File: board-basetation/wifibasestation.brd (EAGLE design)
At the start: 50 x 23 mm, 25 parts, among them J1 SWD_SHROUD_SMD, Q1 MOSFET-PCHANNELSMD

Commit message: some routing
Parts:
- removed C7: (no value), rcl:C0603K
- removed Q1: MOSFET-PCHANNELSMD, SparkFun-DiscreteSemi:SOT23-3
- added C10, C11, C8, C9: (no value), rcl:C0603K
- added IC1: 1117EMP, dtb:SOT223
- added IC2: HTU21D, Mine:DFN6-L
- added R5: (no value), rcl:R0603
- added S1: SWITCH-MOMENTARY-2SMD, Mine:TACTILE_SWITCH_SMD
- added U$4: BUS-SMA, Ava:BUS-SMA
- LED1, LED2, LED3: device dtb:1206 -> led:CHIP-LED0805
- U$3: value CRYSTAL-GROUNDED -> LMT85; device SparkFun-FreqCtrl:CRYSTAL-SMD-5X3 -> Mine:SC70-5L
- moved R1 126.0 mm to (40.4, 8.89), turned to 90 degrees
- moved C6 123.2 mm to (46.2, 2.29)
- moved R2 115.8 mm to (28.4, 3.76), turned to 180 degrees
- moved C4 109.9 mm to (29.8, 16.3), turned to 270 degrees
- moved C5 107.6 mm to (29.3, 8.95), turned to 270 degrees
- moved C3 99.5 mm to (18.0, 18.7)
- moved C1 98.4 mm to (27.4, 8.95), turned to 270 degrees
- moved C2 91.5 mm to (16.5, 10.5), turned to 90 degrees
- moved U$2 24.5 mm to (14.0, 19.4), turned to 180 degrees
- moved U$3 14.8 mm to (35.6, 24.1)
- moved JP3 5.04 mm to (17.7, 21.0)
- moved RN1 4.84 mm to (32.3, 8.38)
- moved LED1 4.67 mm to (36.3, 4.32)
- moved R3 4.19 mm to (15.5, 14.3), turned to 180 degrees
- moved R4 4.12 mm to (8.62, 10.2)
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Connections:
- removed net N$1: SV1.1
- removed net N$6: SV1.7
- new net CH_PD: SV1.6, U$1.5
- new net DIO0: U$1.45, U$2.DIO0
- new net I2C2_SCL: IC2.6, R1.1, U$1.21
- new net I2C2_SDA: IC2.1, R5.1, U$1.22
- new net MISO: U$1.40, U$2.MISO
- new net MOSI: U$1.41, U$2.MOSI
- new net N$19: U$2.ANT, U$4.1
- new net N$20: LED3.A, RN1.5
- new net N$21: RN1.3, U$1.3
- new net N$22: RN1.2, U$1.4
- new net N$23: U$1.29
- new net N$24: U$1.30
- new net N$26: U$1.26
- new net N$27: U$1.27
- new net NSS: U$1.46, U$2.NSS
- new net RST: U$2.RESET
- new net SCK: U$1.39, U$2.SCK
- new net USART1_RX: SV1.8, U$1.43
- new net USART1_TX: SV1.1, U$1.42
- new net USART2_RX: JP3.TXO, U$1.13
- new net USART2_TX: JP3.RXI, U$1.12
- new net W_RST: SV1.4, U$1.6
- net +3V3: now also C10.1, C11.1, C6.1, C9.1, IC1.2, IC1.4, IC2.5, JP3.VCC, R1.2, R5.2, S1.3, SV1.2, U$2.VCC
- net GND: now also C10.2, C11.2, C8.2, C9.2, IC1.1, IC2.2, JP3.GND, LED1.C, LED2.C, LED3.C, SV1.7, U$2.GNDA, U$2.GNDB, U$4.2, U$4.3, U$4.4, U$4.5; no longer C7.2, U$3.2, U$3.4
- net N$10: now also LED2.A, RN1.6; no longer Q1.2
- net N$12: now also U$1.15; no longer C7.1, R1.2, U$3.3
- net N$14: now also U$1.16; no longer R1.1, U$1.6
- net N$15: now also S1.1
- net N$16: now also U$1.17; no longer C6.1, U$1.5, U$3.1
- net N$2: now also RN1.4, U$1.2; no longer Q1.3, SV1.2
- net N$3: now also U$1.10; no longer SV1.4
- net N$7: now also U$1.11; no longer SV1.6
- net N$8: now also U$1.14; no longer SV1.8
- net N$9: now also LED1.A, RN1.7, RN1.8; no longer Q1.1
- net VBUS: now also C8.1, IC1.3
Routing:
- net +3V3: track 0.00 -> 137.7 mm, vias 0 -> 18
- net GND: track 0.00 -> 65.9 mm, vias 0 -> 13
- net NRST: track 0.00 -> 43.6 mm, vias 0 -> 2
- net USART1_RX: track 0.00 -> 43.3 mm, vias 0 -> 2
- net USART1_TX: track 0.00 -> 37.1 mm, vias 0 -> 1
- net I2C2_SCL: track 0.00 -> 37.1 mm, vias 0 -> 4
- net I2C2_SDA: track 0.00 -> 33.1 mm, vias 0 -> 4
- net N$15: track 0.00 -> 32.4 mm, vias 0 -> 2
- net DIO0: track 0.00 -> 21.1 mm, vias 0 -> 1
- net CH_PD: track 0.00 -> 21.0 mm
- net W_RST: track 0.00 -> 20.9 mm, vias 0 -> 1
- net SCK: track 0.00 -> 19.6 mm, vias 0 -> 1
- net N$18: track 0.00 -> 19.5 mm, vias 0 -> 2
- net MISO: track 0.00 -> 18.0 mm, vias 0 -> 1
- net SWDAT: track 0.00 -> 17.6 mm, vias 0 -> 2
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- added copper zone on layer 1, net +3V3
- added copper zone on layer 16, net +3V3
- added copper zone on layer 16, net GND
- added copper zone on layer 16, net N$1
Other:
- board size 50 x 23 mm -> 50 x 22 mm

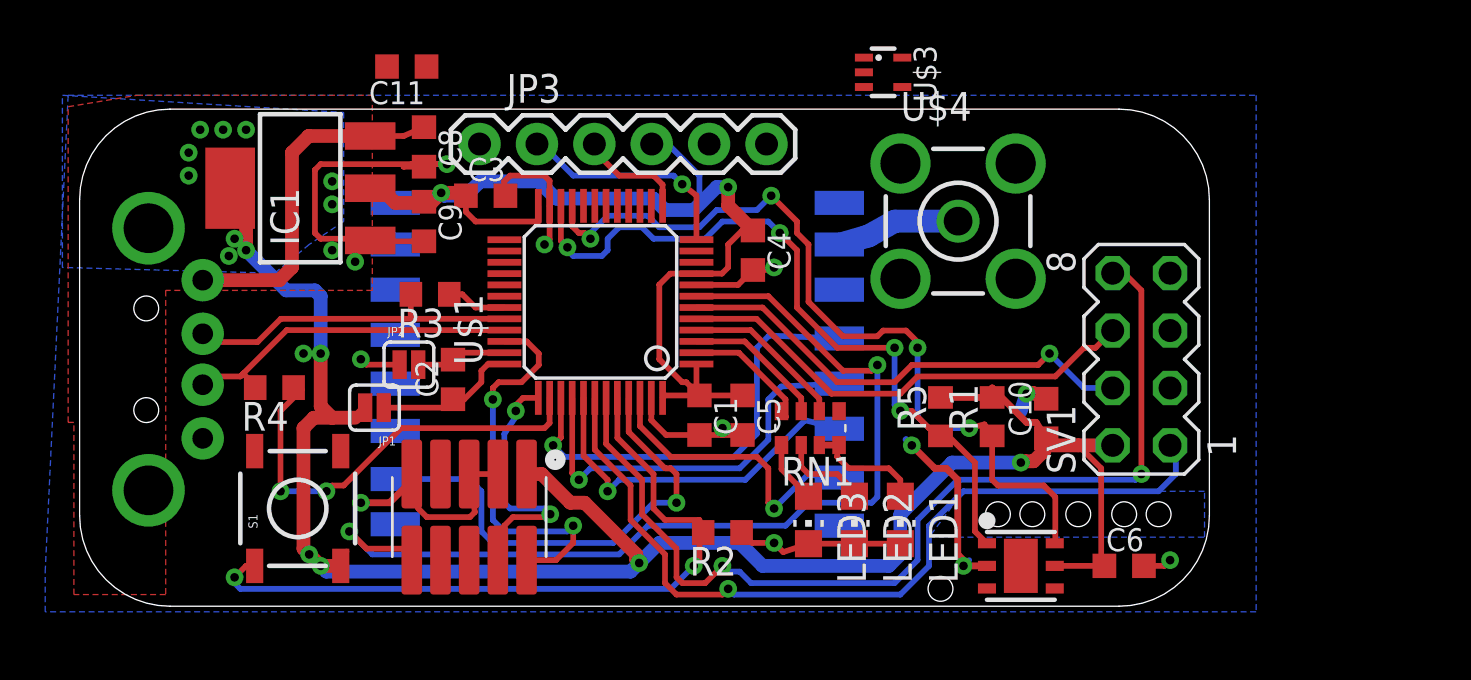
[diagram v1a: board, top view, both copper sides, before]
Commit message: moved to smd esp
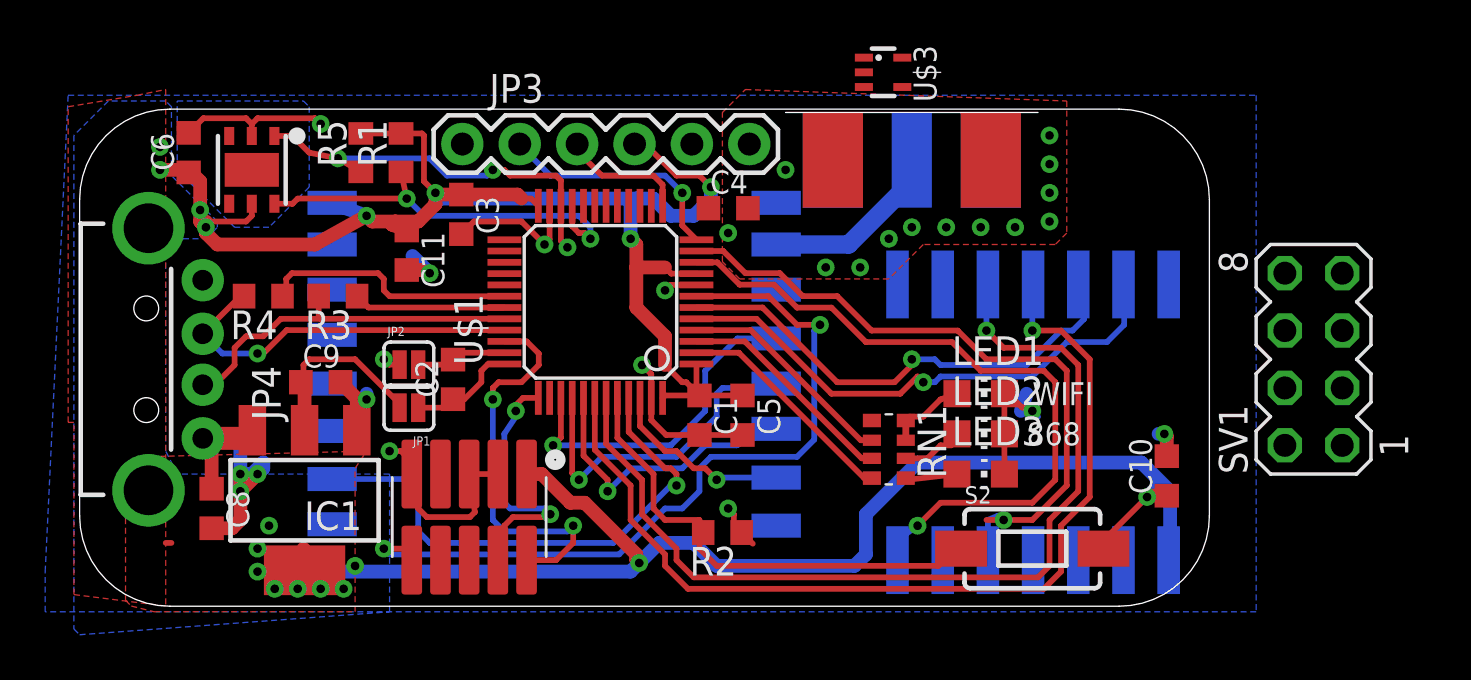
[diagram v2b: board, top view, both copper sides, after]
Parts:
- removed S1: SWITCH-MOMENTARY-2SMD, Mine:TACTILE_SWITCH_SMD
- removed U$4: BUS-SMA, Ava:BUS-SMA
- added S2: SWITCH-MOMENTARY-2SMD-1101NE, SparkFun-Electromechanical:TACTILE-SWITCH-1101NE
- added X1: ESP-03, Mine:ESP-03
- added X2: SMA-142-0711-821/826, con-coax:J502-ND-142-0711-821/826
- moved C6 45.3 mm to (4.83, 20.6), turned to 90 degrees
- moved IC2 38.3 mm to (7.62, 19.8), turned to 180 degrees
- moved R1 28.7 mm to (14.2, 20.6)
- moved R5 28.2 mm to (12.4, 20.6)
- moved C8 18.6 mm to (5.84, 4.83)
- moved IC1 13.8 mm to (9.96, 5.19), turned to 180 degrees
- moved C9 8.45 mm to (10.7, 10.4), turned to 0 degrees
- moved C11 8.13 mm to (14.5, 16.3), turned to 270 degrees
- moved LED3 7.89 mm to (39.9, 6.35), turned to 270 degrees
- moved SV1 7.62 mm to (54.6, 11.4)
- moved LED2 6.76 mm to (39.9, 8.13), turned to 270 degrees
- moved LED1 6.62 mm to (39.9, 9.91), turned to 270 degrees
- moved C10 5.91 mm to (48.1, 6.27)
- moved R3 4.08 mm to (11.4, 14.2)
- moved R4 4.08 mm to (8.13, 14.2)
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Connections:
- removed net N$19: U$2.ANT, U$4.1
- removed net N$23: U$1.29
- removed net N$24: U$1.30
- removed net N$3: U$1.10
- removed net N$4: SV1.3
- removed net N$7: U$1.11
- new net GPIO0: SV1.3, U$1.10, X1.7
- new net GPIO15: U$1.11, X1.5
- new net N$1: X1.6
- new net N$6: U$2.ANT, X2.1
- net +3V3: now also S2.2, X1.1; no longer S1.3
- net CH_PD: now also X1.13
- net GND: now also X1.8, X2.G@1, X2.G@2, X2.G@3, X2.G@4; no longer U$4.2, U$4.3, U$4.4, U$4.5
- net N$15: now also S2.1; no longer S1.1
- net N$18: now also U$1.30; no longer U$1.38
- net USART1_RX: now also X1.10
- net USART1_TX: now also X1.11
- net W_RST: now also X1.12
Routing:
- net GPIO0: track 0.00 -> 31.3 mm, vias 0 -> 1
- net GPIO15: track 0.00 -> 30.4 mm, vias 0 -> 1
- net I2C2_SCL: track 37.1 -> 18.3 mm, vias 4 -> 2
- net I2C2_SDA: track 33.1 -> 18.0 mm, vias 4 -> 3
- net N$15: track 32.4 -> 21.5 mm, vias 2 -> 0
- net VBUS: track 15.5 -> 4.74 mm
- net GND: track 65.9 -> 56.4 mm, vias 13 -> 27
- net NRST: track 43.6 -> 34.6 mm
- net N$18: track 19.5 -> 11.3 mm, vias 2 -> 0
- net N$6: track 0.00 -> 8.09 mm
- net N$19: track 5.48 -> 0.00 mm
- net USART1_TX: track 37.1 -> 42.0 mm
- net NSS: track 13.1 -> 8.30 mm
- net N$2: track 5.90 -> 10.1 mm
- net N$17: track 2.68 -> 6.73 mm
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- added copper zone on layer 1, net GND
- added copper zone on layer 16, net N$19
- removed copper zone on layer 16, net N$1
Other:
- board text added: "868"
- board text added: "WIFI"

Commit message: something changed probably
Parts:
- moved X2 0.17 mm to (36.8, 22.5)
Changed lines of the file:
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@@
 <element name="C6" library="rcl" package="C0603K" value="" x="4.826" y="20.574" rot="R90"/>
 <element name="X1" library="Mine" package="ESP-03" value="ESP-03" x="34.798" y="2.54" rot="MR0"/>
-<element name="X2" library="con-coax" package="J502-ND-142-0711-821/826" value="SMA-142-0711-821/826" x="36.83" y="22.352" rot="MR270">
-<attribute name="OC_NEWARK" value="16F3627" x="36.83" y="22.352" size="1.778" layer="28" rot="MR270" display="off"/>
-<attribute name="MPN" value="142-0711-821" x="36.83" y="22.352" size="1.778" layer="28" rot="MR270" display="off"/>
-<attribute name="MF" value="JOHNSON COMPONENTS" x="36.83" y="22.352" size="1.778" layer="28" rot="MR270" display="off"/>
-<attribute name="OC_FARNELL" value="1019328" x="36.83" y="22.352" size="1.778" layer="28" rot="MR270" display="off"/>
+<element name="X2" library="con-coax" package="J502-ND-142-0711-821/826" value="SMA-142-0711-821/826" x="36.75" y="22.5" rot="MR270">
+<attribute name="OC_NEWARK" value="16F3627" x="36.75" y="22.5" size="1.778" layer="28" rot="MR270" display="off"/>
+<attribute name="MPN" value="142-0711-821" x="36.75" y="22.5" size="1.778" layer="28" rot="MR270" display="off"/>
+<attribute name="MF" value="JOHNSON COMPONENTS" x="36.75" y="22.5" size="1.778" layer="28" rot="MR270" display="off"/>
+<attribute name="OC_FARNELL" value="1019328" x="36.75" y="22.5" size="1.778" layer="28" rot="MR270" display="off"/>
 </element>
 <element name="S2" library="SparkFun-Electromechanical" package="TACTILE-SWITCH-1101NE" value="SWITCH-MOMENTARY-2SMD-1101NE" x="42.164" y="3.048">
@@
 <via x="15.494" y="15.24" extent="1-16" drill="0.381" shape="octagon"/>
 <wire x1="15.494" y1="15.24" x2="14.732" y2="16.002" width="0.6096" layer="16"/>
-<wire x1="12.2674" y1="8.2888" x2="12.2674" y2="9.2194" width="0.6096" layer="1"/>
-<wire x1="12.2674" y1="9.2194" x2="12.7" y2="9.652" width="0.6096" layer="1"/>
-<via x="12.7" y="9.652" extent="1-16" drill="0.381" shape="octagon"/>
-<wire x1="12.7" y1="9.652" x2="12.7" y2="9.906" width="0.6096" layer="16"/>
-<wire x1="12.2674" y1="9.2194" x2="12.2674" y2="9.6896" width="0.6096" layer="1"/>
+<wire x1="12.2674" y1="8.2888" x2="12.2674" y2="9.6896" width="0.6096" layer="1"/>
+<via x="13.208" y="8.128" extent="1-16" drill="0.381" shape="octagon"/>
 <wire x1="12.2674" y1="9.6896" x2="11.543" y2="10.414" width="0.6096" layer="1"/>
 <wire x1="5.842" y1="3.951" x2="6.745" y2="3.951" width="0.6096" layer="1"/>
@@
 <wire x1="7.112" y1="6.35" x2="7.112" y2="7.874" width="0.6096" layer="16"/>
 <wire x1="7.112" y1="6.35" x2="7.112" y2="5.588" width="0.6096" layer="16"/>
-<via x="13.716" y="7.366" extent="1-16" drill="0.381" shape="octagon"/>
+<via x="13.716" y="7.112" extent="1-16" drill="0.381" shape="octagon"/>
 <via x="7.874" y="6.35" extent="1-16" drill="0.381" shape="octagon"/>
 <wire x1="7.112" y1="6.35" x2="7.62" y2="6.35" width="0.6096" layer="16"/>
@@
 <wire x1="8.128" y1="6.604" x2="7.874" y2="6.35" width="0.6096" layer="16"/>
 <wire x1="7.112" y1="5.588" x2="7.874" y2="6.35" width="0.6096" layer="1"/>
-<wire x1="13.716" y1="7.366" x2="14.224" y2="7.366" width="0.254" layer="1"/>
-<wire x1="14.224" y1="7.366" x2="14.478" y2="7.112" width="0.254" layer="1"/>
+<wire x1="13.716" y1="7.112" x2="14.478" y2="7.112" width="0.254" layer="1"/>
 <wire x1="14.478" y1="7.112" x2="14.478" y2="6.572" width="0.254" layer="1"/>
 <wire x1="14.478" y1="6.572" x2="14.7" y2="6.35" width="0.254" layer="1"/>
@@
 <vertex x="29.464" y="23.368"/>
 </polygon>
+<wire x1="13.208" y1="8.128" x2="12.4282" y2="8.128" width="0.254" layer="1"/>
+<wire x1="12.4282" y1="8.128" x2="12.2674" y2="8.2888" width="0.254" layer="1"/>
 <wire x1="48.006" y1="8.128" x2="55.88" y2="15.24" width="0" layer="19" extent="16-16"/>
 </signal>
@@
 <wire x1="5.588" y1="17.018" x2="6.096" y2="16.51" width="0.6096" layer="1"/>
 <wire x1="6.096" y1="16.51" x2="10.414" y2="16.51" width="0.6096" layer="1"/>
-<wire x1="10.414" y1="16.51" x2="12.7" y2="17.78" width="0.6096" layer="1"/>
 <via x="3.556" y="19.812" extent="1-16" drill="0.381" shape="octagon"/>
 <wire x1="3.556" y1="19.812" x2="4.826" y2="19.812" width="0.6096" layer="1"/>
@@
 <wire x1="25.908" y1="11.176" x2="26.67" y2="10.414" width="0.254" layer="1"/>
 <wire x1="48.26" y1="5.588" x2="53.34" y2="7.62" width="0" layer="19" extent="16-16"/>
+<wire x1="12.7" y1="17.78" x2="11.684" y2="17.78" width="0.6096" layer="1"/>
+<wire x1="11.684" y1="17.78" x2="10.414" y2="16.51" width="0.6096" layer="1"/>
 </signal>
 <signal name="N$15">
@@
 <wire x1="34.03625" y1="16.51025" x2="36.576" y2="19.05" width="0.8128" layer="16"/>
 <wire x1="36.576" y1="19.05" x2="36.576" y2="19.9826" width="0.8128" layer="16"/>
-<wire x1="36.576" y1="19.9826" x2="36.83" y2="20.2366" width="0.8128" layer="16"/>
+<wire x1="36.576" y1="19.9826" x2="36.75" y2="20.3846" width="0.8128" layer="16"/>
 </signal>
 <signal name="N$19">

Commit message: routing improved
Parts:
- moved SV1 2.55 mm to (57.1, 11.7), flipped to the bottom
- moved JP1 0.05 mm to (14.6, 9.24), turned to 270 degrees
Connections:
- removed net N$1: X1.6
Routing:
- net +3V3: track 135.3 -> 137.8 mm, vias 18 -> 16
- net NRST: track 34.6 -> 36.0 mm
- net DIO0: track 23.4 -> 22.0 mm
- net SWDAT: track 17.6 -> 16.8 mm

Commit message: pretty much done
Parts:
- removed C11: (no value), rcl:C0603K
- removed U$3: LMT85, Mine:SC70-5L
- added C7: 1u, rcl:C0603
- added IC3: HTU21D, Mine:DFN6-L
- C1, C5: value (none) -> 4u7; device rcl:C0603K -> rcl:C0603
- C10, C2, C3: value (none) -> 1u; device rcl:C0603K -> rcl:C0603
- C4, C8, C9: value (none) -> 100n; device rcl:C0603K -> rcl:C0603
- C6: value (none) -> 100n
- IC2: value HTU21D -> STM32F072; device Mine:DFN6-L -> dtb:TQFP48
- JP3: value FTDI_BASICPTH -> USB-A-H; device SparkFun-Connectors:FTDI_BASIC -> SparkFun-Connectors:USB-A-H
- JP4: value USB-A-H -> FTDI_BASICPTH; device SparkFun-Connectors:USB-A-H -> SparkFun-Connectors:FTDI_BASIC
- R1, R2: value (none) -> 10k
- R3: value (none) -> 100k
- R4, R5: value (none) -> 4k7
- RN1: value (none) -> 330
- U$1: value STM32F072 -> LMT85; device dtb:TQFP48 -> Mine:SC70-5L
- moved C10 45.6 mm to (4.83, 20.6)
- moved C2 31.9 mm to (48.1, 6.27)
- moved R2 22.9 mm to (8.13, 14.2)
- moved R1 22.0 mm to (28.4, 3.76), turned to 180 degrees
- moved C1 22.0 mm to (5.84, 4.83)
- moved C9 19.6 mm to (28.7, 18.1)
- moved C5 18.7 mm to (10.7, 10.4), turned to 0 degrees
- moved C8 17.1 mm to (16.9, 17.8)
- moved JP3 16.8 mm to (3.05, 11.4)
- moved JP4 16.8 mm to (16.9, 21.0)
- moved IC2 16.5 mm to (23.1, 14.0), turned to 90 degrees
- moved U$1 16.1 mm to (35.6, 24.1), turned to 270 degrees
- moved C6 15.4 mm to (16.5, 10.5)
- moved C3 13.8 mm to (27.4, 8.95)
- moved C4 9.18 mm to (29.3, 8.95), turned to 270 degrees
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- renumbered S2 to S1
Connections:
- net +3V3: now also C2.1, C7.1, C8.1, IC2.1, IC2.24, IC2.48, IC2.9, IC3.5, JP4.VCC, R4.2; no longer C1.1, C11.1, C6.1, IC2.5, JP3.VCC, R1.2, U$1.1, U$1.24, U$1.48, U$1.9
- net CH_PD: now also IC2.5; no longer U$1.5
- net DIO0: now also IC2.45; no longer U$1.45
- net DM: now also IC2.32, JP3.D-; no longer JP4.D-, U$1.32
- net DP: now also IC2.33, JP3.D+, R2.2; no longer JP4.D+, R4.2, U$1.33
- net GND: now also C2.2, C7.2, IC2.23, IC2.47, IC2.8, IC3.2, R1.1; no longer C11.2, C6.2, IC2.2, R2.1, U$1.23, U$1.47, U$1.8
- net GPIO0: now also IC2.10; no longer U$1.10
- net GPIO15: now also IC2.11; no longer U$1.11
- net I2C2_SCL: now also IC2.21, IC3.6, R5.1; no longer IC2.6, R1.1, U$1.21
- net I2C2_SDA: now also IC2.22, IC3.1, R4.1; no longer IC2.1, R5.1, U$1.22
- net MISO: now also IC2.40; no longer U$1.40
- net MOSI: now also IC2.41; no longer U$1.41
- net N$10: now also RN1.7; no longer RN1.6
- net N$11: now also C6.1, IC2.36; no longer C2.1, U$1.36
- net N$12: now also IC2.15; no longer U$1.15
- net N$13: now also C6.2, IC2.35; no longer C2.2, U$1.35
- net N$14: now also IC2.16; no longer U$1.16
- net N$15: now also IC2.44, R1.2; no longer R2.2, U$1.44
- net N$16: now also IC2.17; no longer U$1.17
- net N$17: now also IC2.31; no longer U$1.31
- net N$18: now also IC2.30, R2.1; no longer R4.1, U$1.30
- net N$2: now also IC2.2, RN1.3; no longer RN1.4, U$1.2
- net N$20: now also LED1.A, RN1.6; no longer LED3.A, RN1.5
- net N$21: now also IC2.3, RN1.2; no longer RN1.3, U$1.3
- net N$22: now also IC2.4, RN1.1; no longer RN1.2, U$1.4
- net N$26: now also IC2.26; no longer U$1.26
- net N$27: now also IC2.27; no longer U$1.27
- net N$8: now also IC2.14; no longer U$1.14
- net N$9: now also LED3.A; no longer LED1.A, RN1.7
- net NRST: now also IC2.7; no longer U$1.7
- net NSS: now also IC2.46; no longer U$1.46
- net SCK: now also IC2.39; no longer U$1.39
- net SWCLK: now also IC2.37; no longer U$1.37
- net SWDAT: now also IC2.34; no longer U$1.34
- net USART1_RX: now also IC2.43; no longer U$1.43
- net USART1_TX: now also IC2.42; no longer U$1.42
- net USART2_RX: now also IC2.13, JP4.TXO; no longer JP3.TXO, U$1.13
- net USART2_TX: now also IC2.12, JP4.RXI; no longer JP3.RXI, U$1.12
- net VBUS: now also C1.1, JP3.VBUS; no longer C8.1, JP4.VBUS
- net W_RST: now also IC2.6; no longer U$1.6
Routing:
- net +3V3: track 137.8 -> 146.9 mm, vias 16 -> 15
- net GPIO0: track 31.3 -> 38.2 mm
- net GPIO15: track 30.4 -> 36.4 mm
- net GND: track 56.4 -> 58.4 mm, vias 27 -> 33
- net SCK: track 16.2 -> 14.7 mm
- net NRST: track 36.0 -> 35.1 mm
- net USART1_TX: track 42.0 -> 41.5 mm
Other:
- board size 50 x 22 mm -> 49.8 x 22 mm
- board text added: "IC3"
